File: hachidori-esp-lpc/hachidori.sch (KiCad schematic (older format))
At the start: 49 parts, among them P1 VIN, P2 UART, P3 ADC, P4 I2C, SW1 FLASH, SW2 RESET, U1 NCP1117ST33, U2 MPU-9250, U3 ESP-13-WROOM-02, U4 BME280, U7 INA226

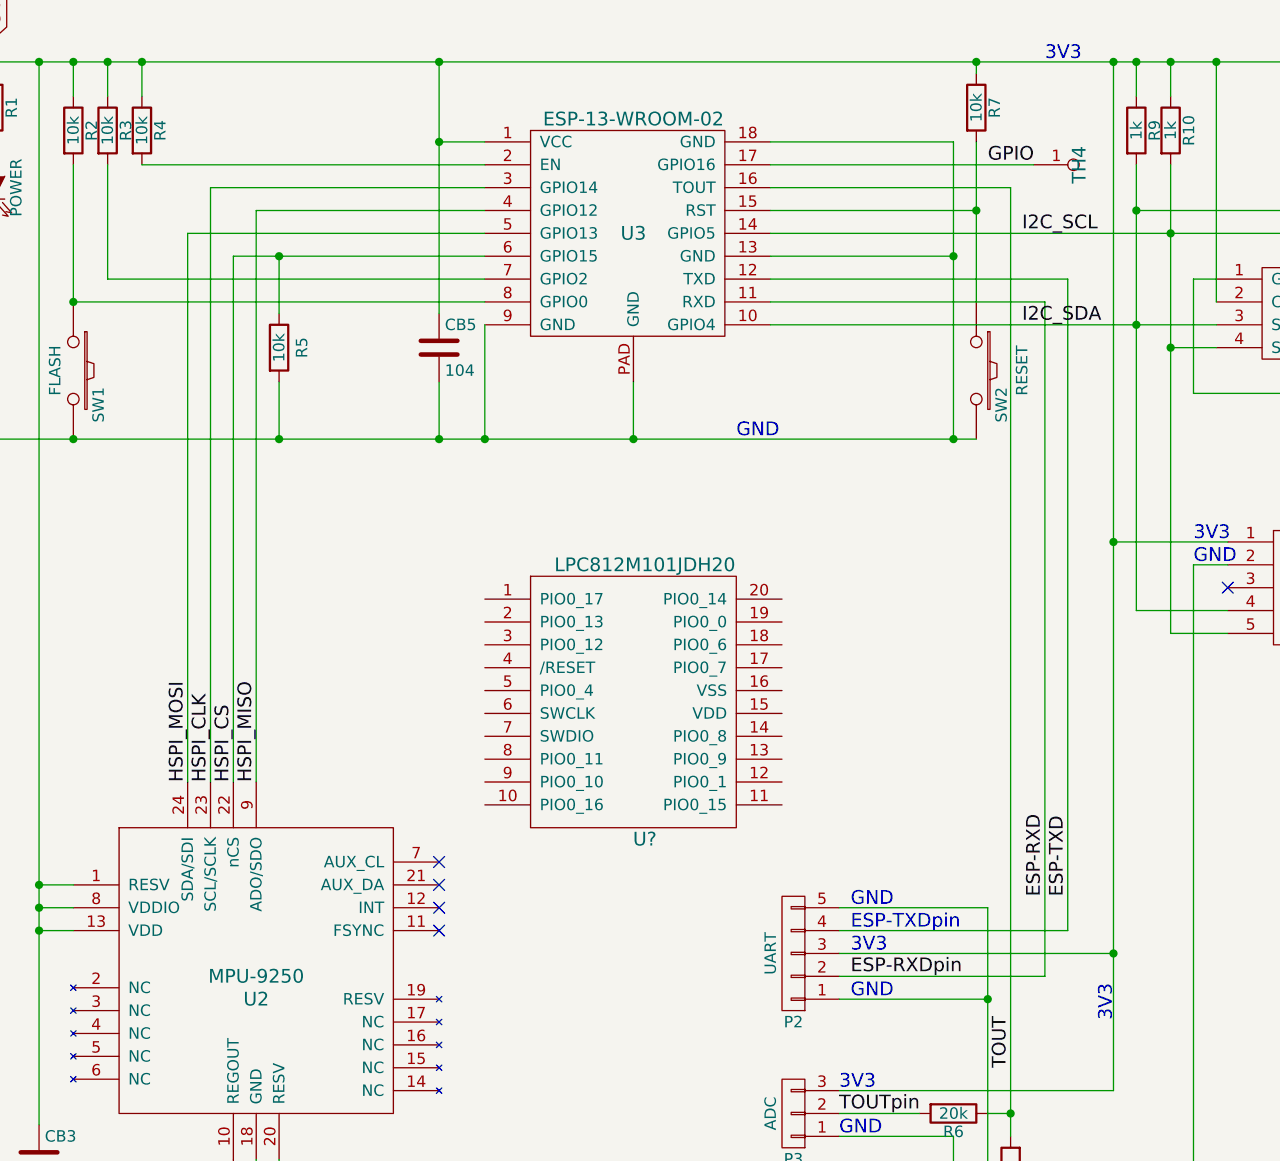
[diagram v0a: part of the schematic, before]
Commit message: connect LPC to esp using SPI
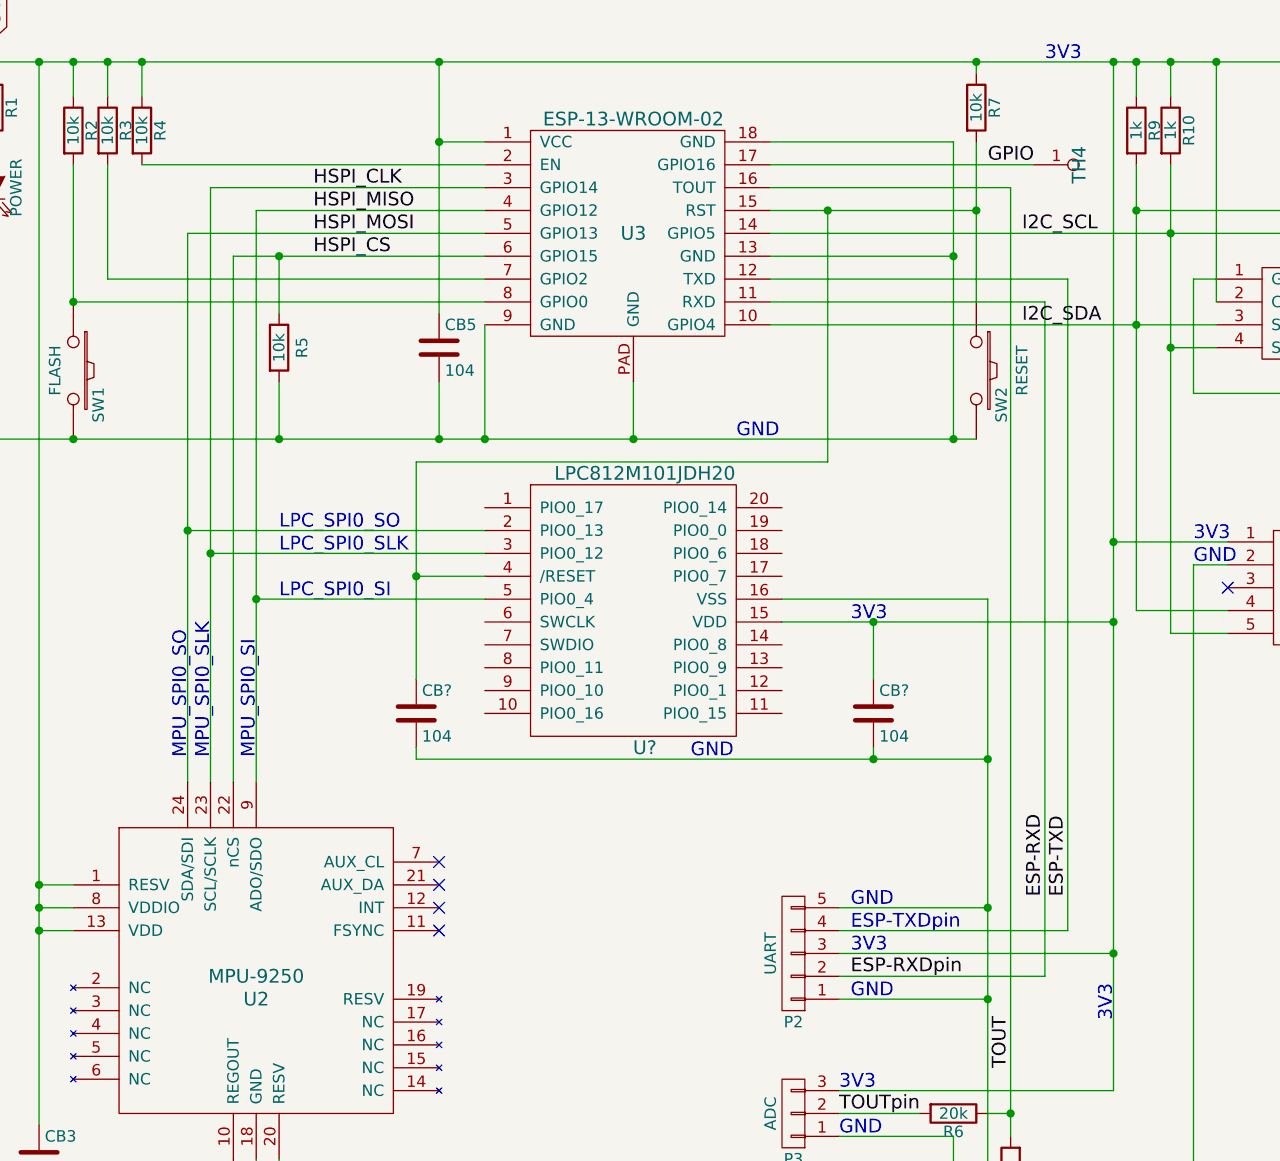
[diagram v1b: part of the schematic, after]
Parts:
- added CB? (x2): 104, droneworks:GRM18, symbol C
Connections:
- net 3V3: now also U?.15 (VDD), CB?.1
- net GND: now also U?.16 (VSS), CB?.2, CB?.2
- net HSPI_CLK: now also U?.3 (PIO0_12)
- net HSPI_MISO: now also U?.5 (PIO0_4)
- net HSPI_MOSI: now also U?.2 (PIO0_13)
- net at R7.2, SW2.1, U3.15 (RST): now also U?.4 (/RESET), CB?.1
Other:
- note added: "LPC_SPI0_SI"
- note added: "LPC_SPI0_SLK"
- note added: "LPC_SPI0_SO"
- note added: "MPU_SPI0_SI"
- note added: "MPU_SPI0_SLK"
- note added: "MPU_SPI0_SO"
- moved on the sheet: U?

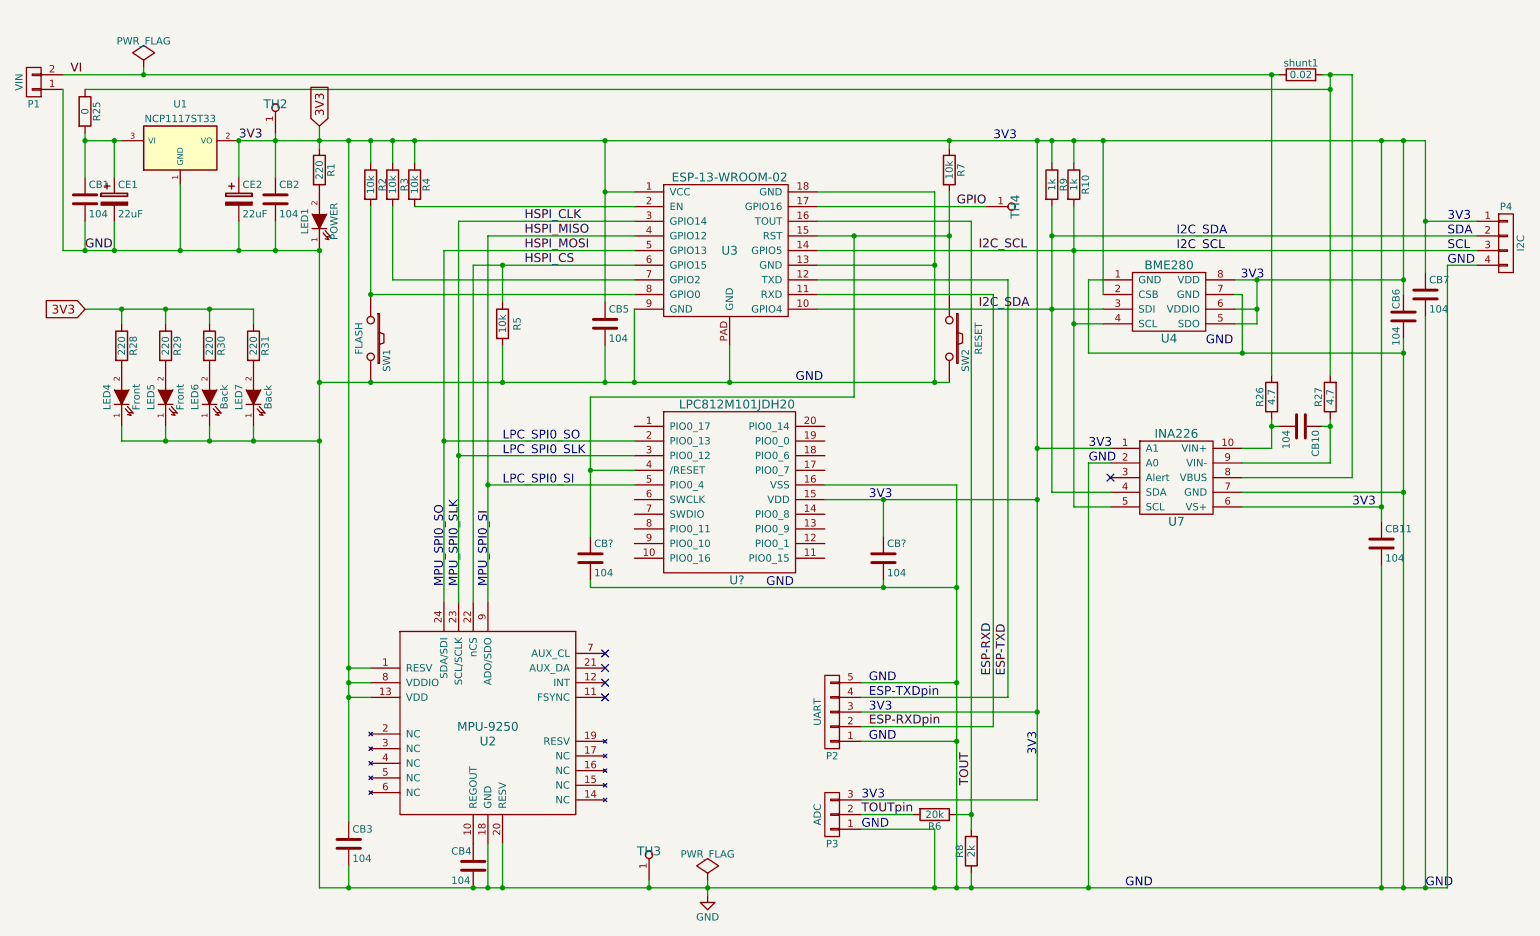
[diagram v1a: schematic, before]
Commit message: add a demultiplexer for chip select
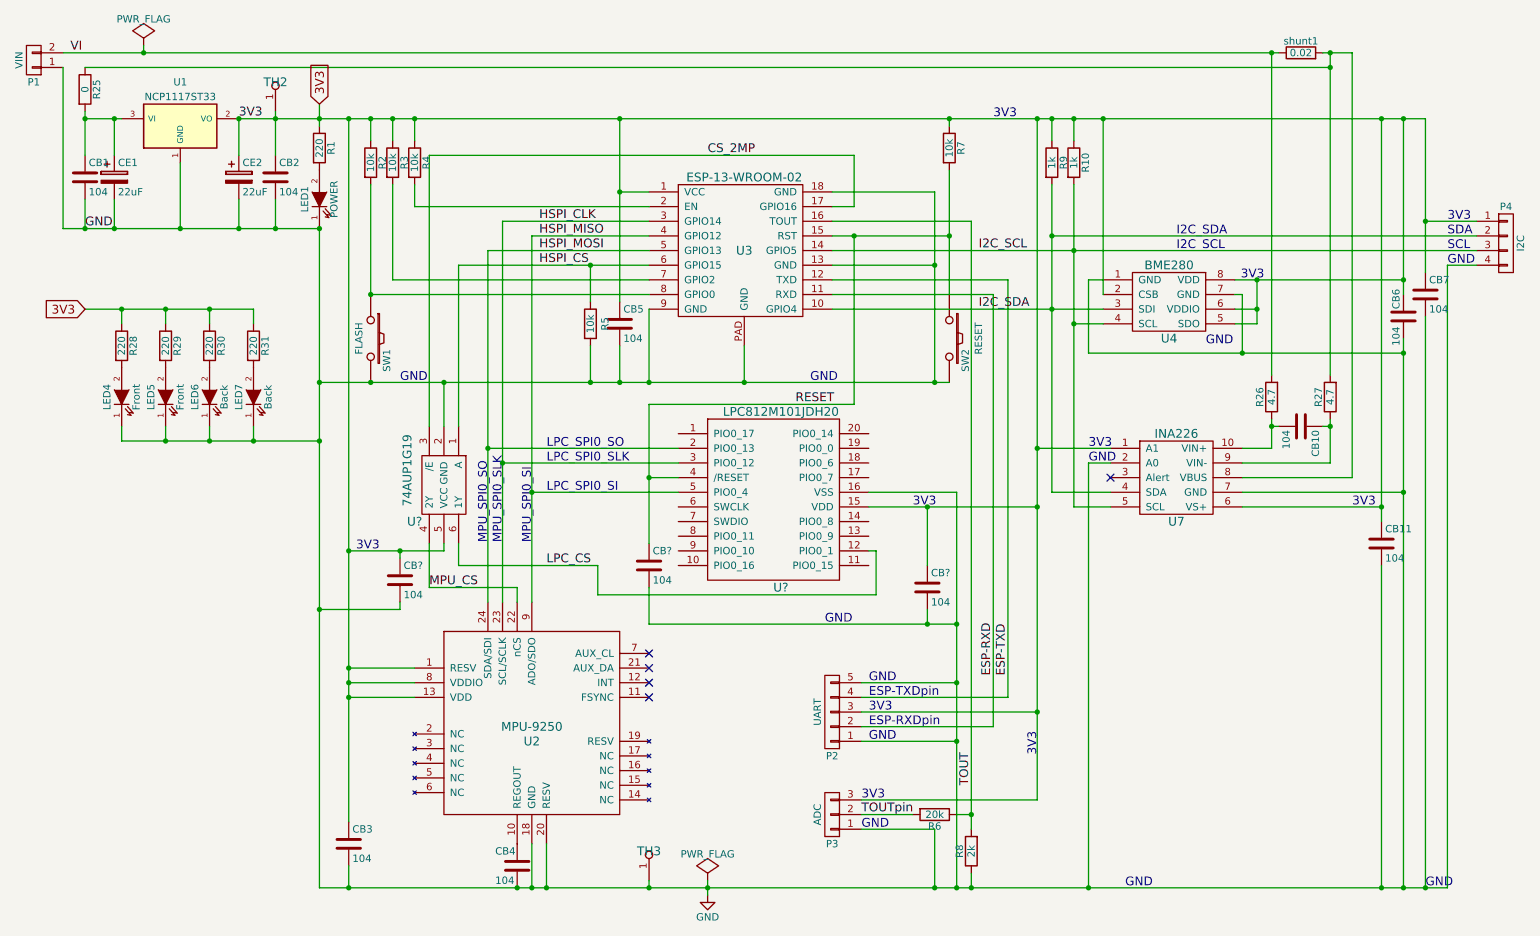
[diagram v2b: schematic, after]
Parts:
- removed TH4: GPIO, droneworks:TH, symbol throughhole
- added CB?: 104, droneworks:GRM18, symbol C
- added U?: 74AUP1G19, symbol 74AUP1G19
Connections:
- net 3V3: now also CB?.1, U?.5 (VCC)
- net GND: now also CB?.2, U?.2 (GND)
- net HSPI_CS: now also U?.1 (A); no longer U2.22 (nCS)
- net RESET: now reaches CB?.1, R7.2, SW2.1, U3.15 (RST), U?.4 (/RESET)
- net LPC_CS: now reaches U?.12 (PIO0_1)
- net LPC_CS: now also U?.6 (1Y)
- net GPIO renamed CS_2MP
- net CS_2MP: now also U?.3 (/E)
- new net MPU_CS: U2.22 (nCS), U?.4 (2Y)
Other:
- note added: "ESP-RXDpin"
- moved on the sheet: CB1, CB2, CB4, CB5, CB?, CE1, CE2, LED1, P1, R1, R10, R2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

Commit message: add SWD interface
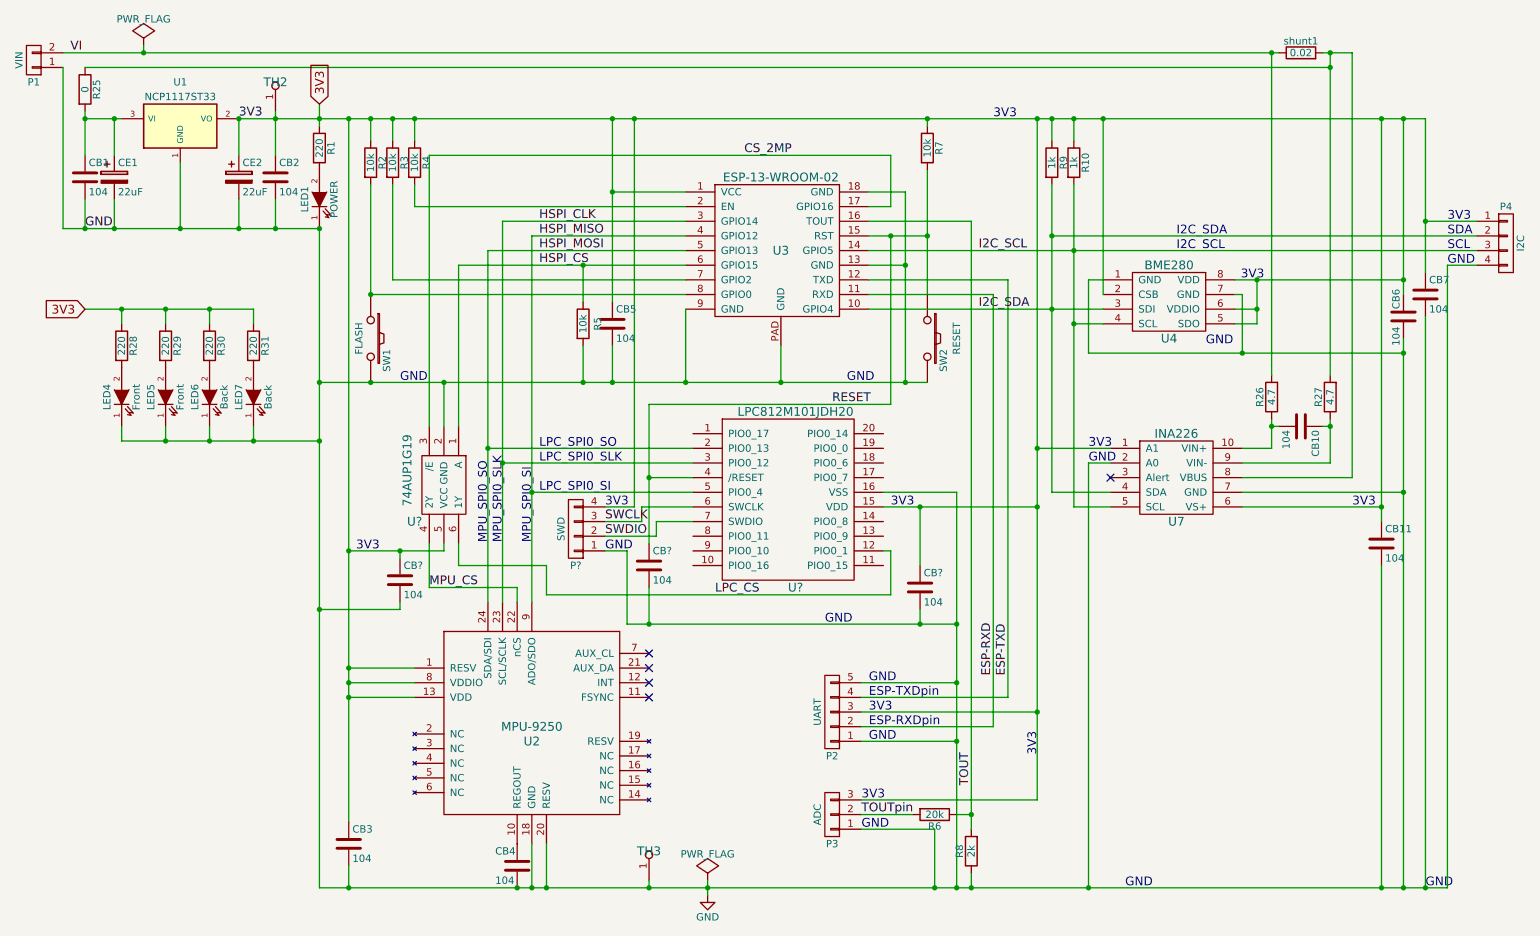
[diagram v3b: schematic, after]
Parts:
- added P?: SWD, symbol CONN_01X04
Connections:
- net 3V3: now also P?.4 (P4)
- net GND: now also P?.1 (P1)
- net SWCLK: now reaches U?.6 (SWCLK)
- net SWCLK: now also P?.3 (P3)
- net SWDIO: now reaches U?.7 (SWDIO)
- net SWDIO: now also P?.2 (P2)
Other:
- moved on the sheet: CB5, CB?, R5, R7, SW2, U3, U?
